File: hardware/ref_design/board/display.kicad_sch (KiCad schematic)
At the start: 11 parts, among them J3 FH12-50S-0.5SH(55), U6 AP3156FVG-7

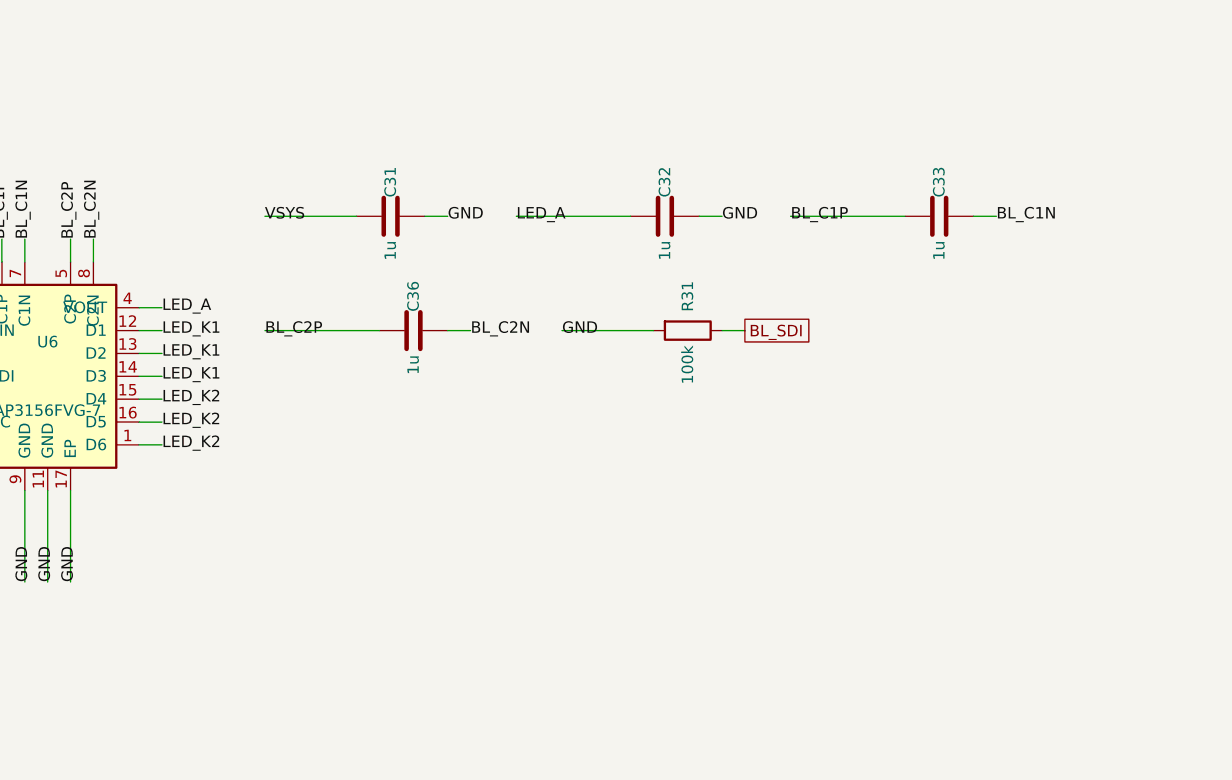
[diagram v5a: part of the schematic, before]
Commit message: Reference design: checklist changes and the datasheet pin gate
Board: PWR_HOLD pull-down (R42, also covers RP2350-E9), charge current
3.3k (333-364 mA), firmware charge pause (CHG_OFF, Q4), R13 33k, 0.1 ohm
in D5's path, JP1/JP2 cut-jumpers, TP6-8, spare 1206 footprints, 4-bit
revision strap on GPIO22-25 (REV 1 on the back).

Datasheet review of every part's pins (pin_review/, tools/check_pins.py)
found and fixed: J6 TX/RX swapped against Raspberry Pi's debug connector
spec, USB series resistors 22 to 27 ohm, the ME6211 CE able to lead its
VIN at a live plug-in (C47 on PWR_EN).

Case: silicone height 1.2 mm from the DS Lite, chamfered step.

Co-Authored-By: Claude Opus 5.5 <noreply@anthropic.com>
Claude-Session: https://claude.ai/code/session_01MUt6paNsT75sqwAr83zRS3
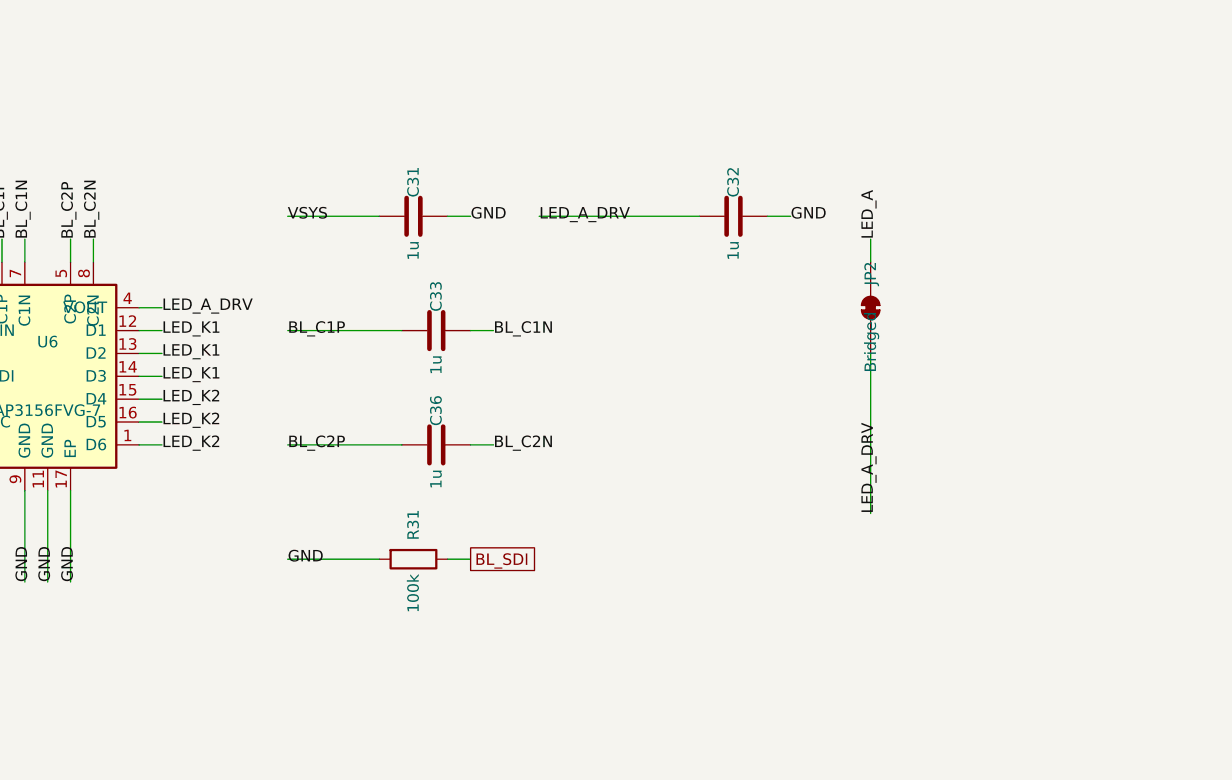
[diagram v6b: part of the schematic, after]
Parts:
- added JP2: Bridged, Jumper:SolderJumper-2_P1.3mm_Bridged_Pad1.0x1.5mm, symbol Jumper:SolderJumper_2_Bridged
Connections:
- net LED_A: now also JP2.2 (B); no longer C32.1, U6.4 (VOUT)
- new net LED_A_DRV: C32.1, JP2.1 (A), U6.4 (VOUT)
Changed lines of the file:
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@@
   (wire
     (pts
-      (xy 166.37 86.36)
-      (xy 156.21 86.36))
-)
-  (wire
-    (pts
-      (xy 173.99 86.36)
-      (xy 176.53 86.36))
-)
-  (wire
-    (pts
-      (xy 196.85 86.36)
-      (xy 184.15 86.36))
+      (xy 168.91 86.36)
+      (xy 158.75 86.36))
+)
+  (wire
+    (pts
+      (xy 176.53 86.36)
+      (xy 179.07 86.36))
 )
   (wire
     (pts
       (xy 204.47 86.36)
-      (xy 207.01 86.36))
-)
-  (wire
-    (pts
-      (xy 227.33 86.36)
+      (xy 186.69 86.36))
+)
+  (wire
+    (pts
+      (xy 212.09 86.36)
       (xy 214.63 86.36))
 )
   (wire
     (pts
-      (xy 234.95 86.36)
-      (xy 237.49 86.36))
-)
-  (wire
-    (pts
-      (xy 168.91 99.06)
-      (xy 156.21 99.06))
-)
-  (wire
-    (pts
-      (xy 176.53 99.06)
-      (xy 179.07 99.06))
-)
-  (wire
-    (pts
-      (xy 207.01 99.06)
-      (xy 209.55 99.06))
-)
-  (wire
-    (pts
-      (xy 199.39 99.06)
-      (xy 189.23 99.06))
+      (xy 223.52 91.44)
+      (xy 223.52 88.9))
+)
+  (wire
+    (pts
+      (xy 223.52 101.6)
+      (xy 223.52 119.38))
+)
+  (wire
+    (pts
+      (xy 171.45 99.06)
+      (xy 158.75 99.06))
+)
+  (wire
+    (pts
+      (xy 179.07 99.06)
+      (xy 181.61 99.06))
+)
+  (wire
+    (pts
+      (xy 171.45 111.76)
+      (xy 158.75 111.76))
+)
+  (wire
+    (pts
+      (xy 179.07 111.76)
+      (xy 181.61 111.76))
+)
+  (wire
+    (pts
+      (xy 176.53 124.46)
+      (xy 179.07 124.46))
+)
+  (wire
+    (pts
+      (xy 168.91 124.46)
+      (xy 158.75 124.46))
 )
   (wire
@@
     (at 137.16 88.9 90)
 )
-  (label "LED_A"
+  (label "LED_A_DRV"
     (at 144.78 96.52 0)
 )
@@
 )
   (label "VSYS"
-    (at 156.21 86.36 0)
-)
-  (label "GND"
-    (at 176.53 86.36 0)
+    (at 158.75 86.36 0)
+)
+  (label "GND"
+    (at 179.07 86.36 0)
+)
+  (label "LED_A_DRV"
+    (at 186.69 86.36 0)
+)
+  (label "GND"
+    (at 214.63 86.36 0)
 )
   (label "LED_A"
-    (at 184.15 86.36 0)
-)
-  (label "GND"
-    (at 207.01 86.36 0)
+    (at 223.52 88.9 90)
+)
+  (label "LED_A_DRV"
+    (at 223.52 119.38 90)
 )
   (label "BL_C1P"
-    (at 214.63 86.36 0)
+    (at 158.75 99.06 0)
 )
   (label "BL_C1N"
-    (at 237.49 86.36 0)
+    (at 181.61 99.06 0)
 )
   (label "BL_C2P"
-    (at 156.21 99.06 0)
+    (at 158.75 111.76 0)
 )
   (label "BL_C2N"
-    (at 179.07 99.06 0)
-)
-  (label "GND"
-    (at 189.23 99.06 0)
+    (at 181.61 111.76 0)
+)
+  (label "GND"
+    (at 158.75 124.46 0)
 )
   (label "GND"
@@
   (global_label "BL_SDI"
     (shape passive)
-    (at 209.55 99.06 0)
+    (at 179.07 124.46 0)
 )
   (symbol
@@
   (symbol
     (lib_id "Device:C")
-    (at 170.18 86.36 90)
+    (at 172.72 86.36 90)
     (unit 1)
     (in_bom yes)
@@
     (dnp no)
     (property "Reference" "C31"
-      (at 170.18 82.55 0)
+      (at 172.72 82.55 0)
       (effects
         (font
           (size 1.27 1.27))))
     (property "Value" "1u"
-      (at 170.18 90.17 0)
+      (at 172.72 90.17 0)
       (effects
         (font
           (size 1.27 1.27))))
     (property "Footprint" "Capacitor_SMD:C_0402_1005Metric"
-      (at 170.18 86.36 0)
-      (effects
-        (font
-          (size 1.27 1.27))
-        (hide yes)))
-    (property "Datasheet" ""
-      (at 170.18 86.36 0)
+      (at 172.72 86.36 0)
+      (effects
+        (font
+          (size 1.27 1.27))
+        (hide yes)))
+    (property "Datasheet" ""
+      (at 172.72 86.36 0)
       (effects
         (font
@@
   (symbol
     (lib_id "Device:C")
-    (at 200.66 86.36 90)
+    (at 208.28 86.36 90)
     (unit 1)
     (in_bom yes)
@@
     (dnp no)
     (property "Reference" "C32"
-      (at 200.66 82.55 0)
+      (at 208.28 82.55 0)
       (effects
         (font
           (size 1.27 1.27))))
     (property "Value" "1u"
-      (at 200.66 90.17 0)
+      (at 208.28 90.17 0)
       (effects
         (font
           (size 1.27 1.27))))
     (property "Footprint" "Capacitor_SMD:C_0402_1005Metric"
-      (at 200.66 86.36 0)
-      (effects
-        (font
-          (size 1.27 1.27))
-        (hide yes)))
-    (property "Datasheet" ""
-      (at 200.66 86.36 0)
+      (at 208.28 86.36 0)
+      (effects
+        (font
+          (size 1.27 1.27))
+        (hide yes)))
+    (property "Datasheet" ""
+      (at 208.28 86.36 0)
       (effects
         (font
@@
           (unit 1)))))
   (symbol
+    (lib_id "Jumper:SolderJumper_2_Bridged")
+    (at 223.52 96.52 90)
+    (unit 1)
+    (in_bom yes)
+    (on_board yes)
+    (dnp no)
+    (property "Reference" "JP2"
+      (at 223.52 92.71 0)
+      (effects
+        (font
+          (size 1.27 1.27))))
+    (property "Value" "Bridged"
+      (at 223.52 100.33 0)
+      (effects
+        (font
+          (size 1.27 1.27))))
+    (property "Footprint" "Jumper:SolderJumper-2_P1.3mm_Bridged_Pad1.0x1.5mm"
+      (at 223.52 96.52 0)
+      (effects
+        (font
+          (size 1.27 1.27))
+        (hide yes)))
+    (property "Datasheet" ""
+      (at 223.52 96.52 0)
+      (effects
+        (font
+          (size 1.27 1.27))
+        (hide yes)))
+    (property "BOM" "exclude"
+      (at 0 0 0)
+      (effects
+        (font
+          (size 1.27 1.27))
+        (hide yes)))
+    (instances
+      (project ""
+        (path "/"
+          (reference "JP2")
+          (unit 1)))))
+  (symbol
     (lib_id "Device:C")
-    (at 231.14 86.36 90)
+    (at 175.26 99.06 90)
     (unit 1)
     (in_bom yes)
@@
     (dnp no)
     (property "Reference" "C33"
-      (at 231.14 82.55 0)
+      (at 175.26 95.25 0)
       (effects
         (font
           (size 1.27 1.27))))
     (property "Value" "1u"
-      (at 231.14 90.17 0)
+      (at 175.26 102.87 0)
       (effects
         (font
           (size 1.27 1.27))))
     (property "Footprint" "Capacitor_SMD:C_0402_1005Metric"
-      (at 231.14 86.36 0)
-      (effects
-        (font
-          (size 1.27 1.27))
-        (hide yes)))
-    (property "Datasheet" ""
-      (at 231.14 86.36 0)
+      (at 175.26 99.06 0)
+      (effects
+        (font
+          (size 1.27 1.27))
+        (hide yes)))
+    (property "Datasheet" ""
+      (at 175.26 99.06 0)
       (effects
         (font
@@
   (symbol
     (lib_id "Device:C")
-    (at 172.72 99.06 90)
+    (at 175.26 111.76 90)
     (unit 1)
     (in_bom yes)
@@
     (dnp no)
     (property "Reference" "C36"
-      (at 172.72 95.25 0)
+      (at 175.26 107.95 0)
       (effects
         (font
           (size 1.27 1.27))))
     (property "Value" "1u"
-      (at 172.72 102.87 0)
+      (at 175.26 115.57 0)
       (effects
         (font
           (size 1.27 1.27))))
     (property "Footprint" "Capacitor_SMD:C_0402_1005Metric"
-      (at 172.72 99.06 0)
-      (effects
-        (font
-          (size 1.27 1.27))
-        (hide yes)))
-    (property "Datasheet" ""
-      (at 172.72 99.06 0)
+      (at 175.26 111.76 0)
+      (effects
+        (font
+          (size 1.27 1.27))
+        (hide yes)))
+    (property "Datasheet" ""
+      (at 175.26 111.76 0)
       (effects
         (font
@@
   (symbol
     (lib_id "Device:R")
-    (at 203.2 99.06 270)
+    (at 172.72 124.46 270)
     (unit 1)
     (in_bom yes)
@@
     (dnp no)
     (property "Reference" "R31"
-      (at 203.2 95.25 0)
+      (at 172.72 120.65 0)
       (effects
         (font
           (size 1.27 1.27))))
     (property "Value" "100k"
-      (at 203.2 102.87 0)
+      (at 172.72 128.27 0)
       (effects
         (font
           (size 1.27 1.27))))
     (property "Footprint" "Resistor_SMD:R_0402_1005Metric"
-      (at 203.2 99.06 0)
-      (effects
-        (font
-          (size 1.27 1.27))
-        (hide yes)))
-    (property "Datasheet" ""
-      (at 203.2 99.06 0)
-      (effects
-        (font
+      (at 172.72 124.46 0)
+      (effects
+        (font
+          (size 1.27 1.27))
+        (hide yes)))
+    (property "Datasheet" ""
+      (at 172.72 124.46 0)
+      (effects
+        (font
